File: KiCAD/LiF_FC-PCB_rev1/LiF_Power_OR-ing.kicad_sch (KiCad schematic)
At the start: 16 parts, among them Q1 IRLML6344TRPbF, Q2 IRLML6344TRPbF, U1 LM5050-1, U2 LM5050-1

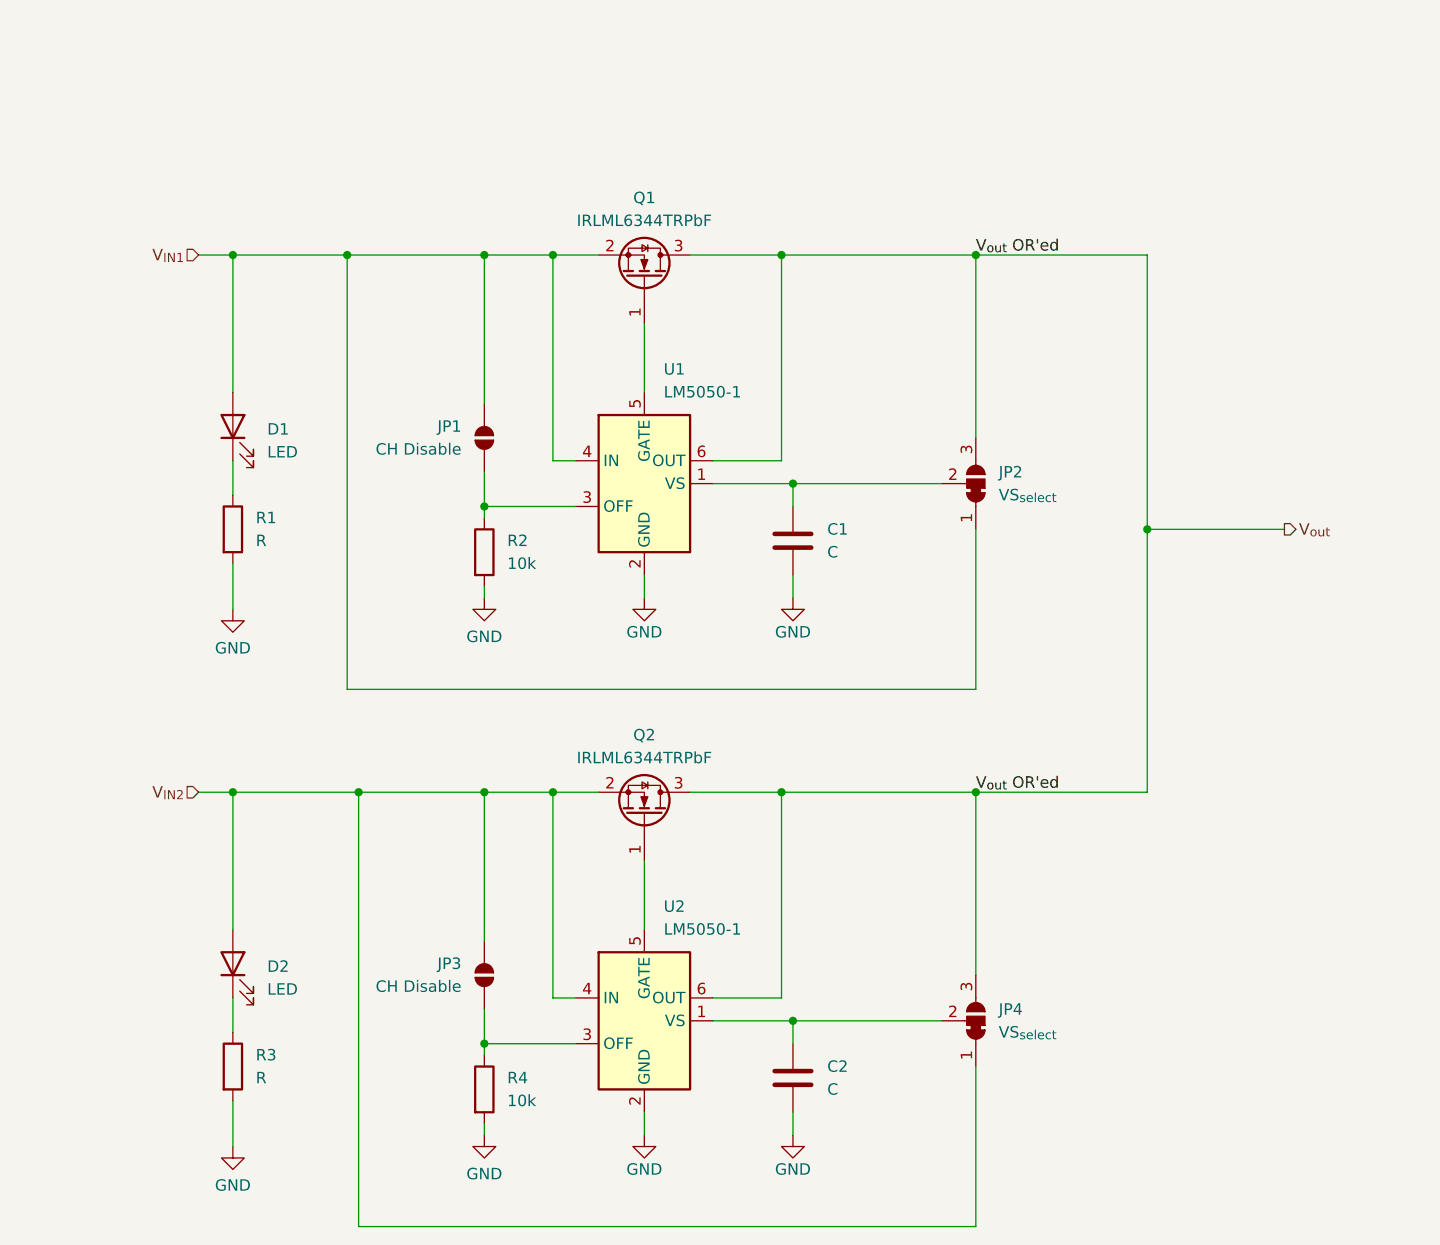
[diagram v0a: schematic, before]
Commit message: reverted 5V reg, reworked power distribution logic, swapped power OR-ing ICs
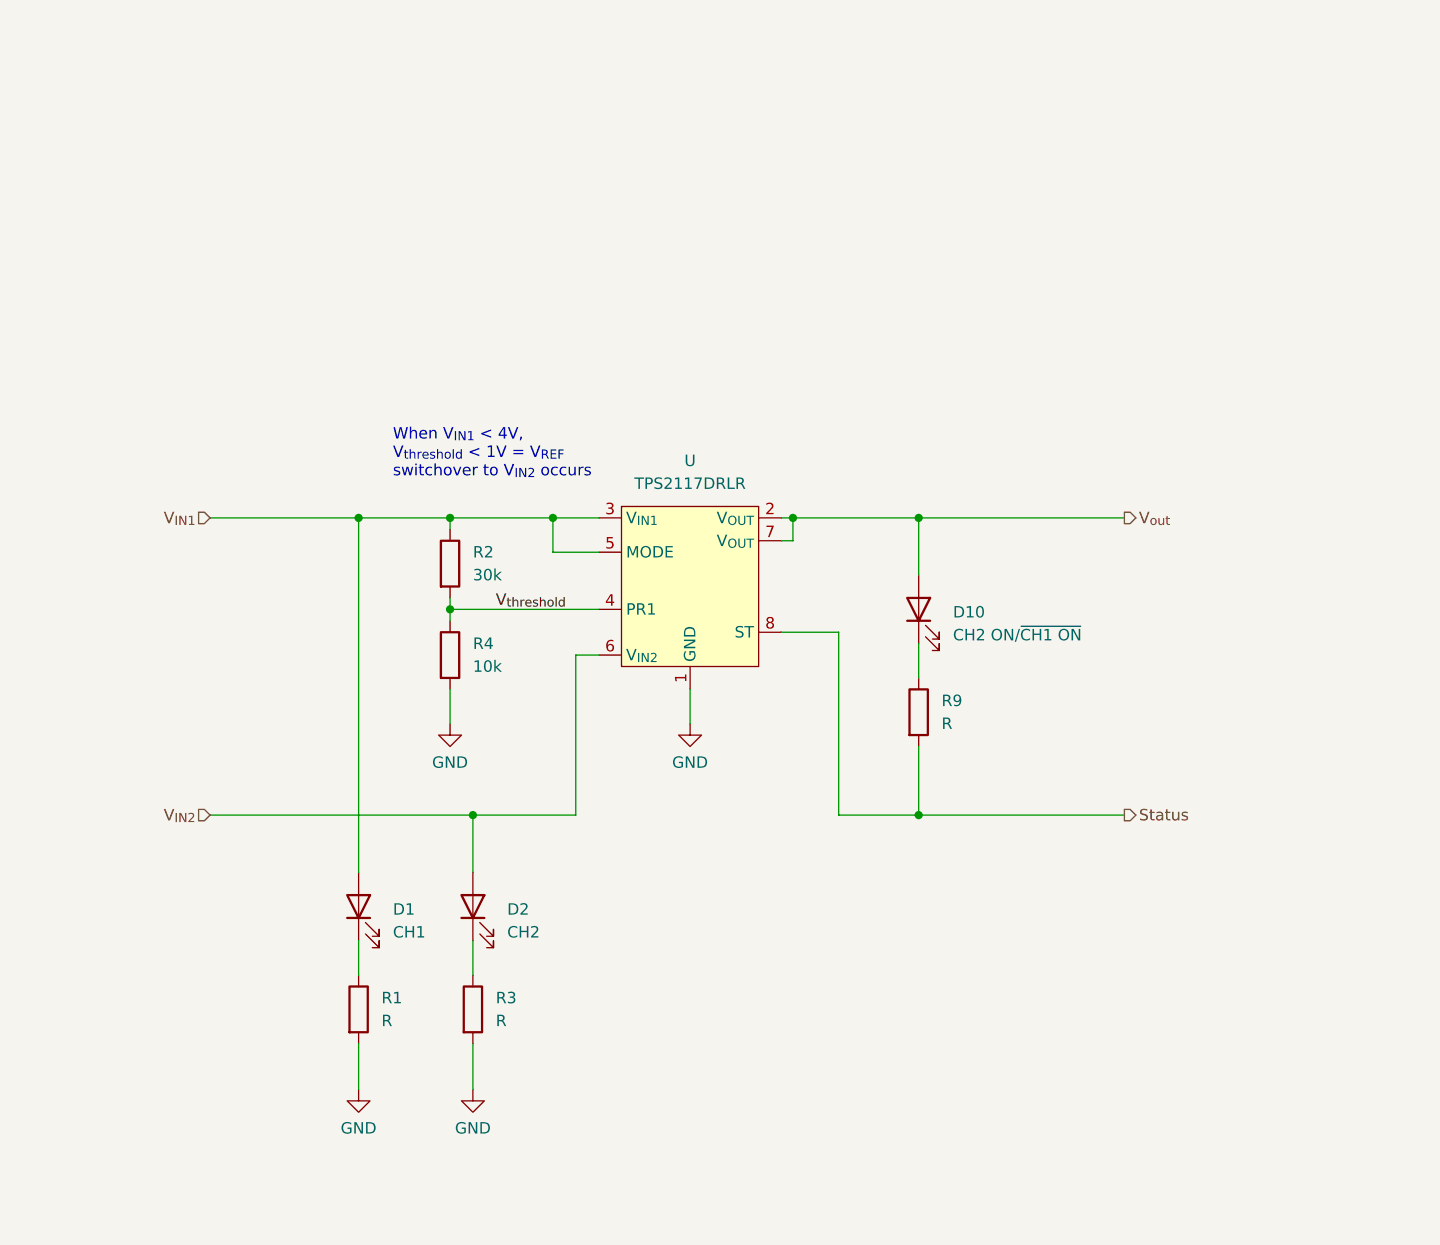
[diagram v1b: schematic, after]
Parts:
- removed C1, C2: C, symbol Device:C
- removed JP1, JP3: CH Disable, symbol Jumper:SolderJumper_2_Open
- removed JP2, JP4: VS_{select}, Jumper:SolderJumper-3_P1.3mm_Bridged12_Pad1.0x1.5mm, symbol Jumper:SolderJumper_3_Bridged12
- removed Q1, Q2: IRLML6344TRPbF, Package_TO_SOT_SMD:SOT-23, symbol Transistor_FET:IRLML6244
- removed U1, U2: LM5050-1, Package_TO_SOT_SMD:TSOT-23-6, symbol Power_Management:LM5050-1
- added D10: CH2 ON/~{CH1 ON}, symbol Device:LED
- added R9: R, symbol Device:R
- added U: TPS2117DRLR, LiF_PCB_Footprints:SOT-5x3_DRL0008A_TEX, symbol LiF_PCB_Symbols:TPS2117
- D1: value LED -> CH1
- D2: value LED -> CH2
- R2: value 10k -> 30k
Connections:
- net GND: now also U.1 (GND); no longer R2.2
- net V_{IN1}: now also R2.1, U.3 (V_{IN1}), U.5 (MODE)
- net V_{IN2}: now also U.6 (V_{IN2})
- net V_{out}: now also D10.2 (A), U.2 (V_{OUT}), U.7 (V_{OUT})
- net V_{threshold}: now reaches R4.1
- net V_{threshold}: now also R2.2, U.4 (PR1)
- new net: D10.1 (K), R9.1
- new net Status: R9.2, U.8 (ST)
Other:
- note added: "When V_{IN1} < 4V, V_{threshold} < 1V = V_{REF} switchover to V_{IN2} occurs"
- moved on the sheet: D1, D2, R1, R3

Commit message: starting to merge Nick's schematics into the main KiCAD project
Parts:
- renumbered U to U?
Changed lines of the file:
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@@
 		(dnp no)
 		(fields_autoplaced yes)
-		(property "Reference" "U"
+		(property "Reference" "U?"
 			(at 146.05 66.04 0)
 			(effects
@@
 		(instances
 			(project "LiF_FC-PCB_rev1"
+				(path "/9e3e8da7-e506-46c9-90e5-307e4ad30d29/dbf56dc2-3990-4801-b0e0-f59d351af64c/b5f6c072-28d6-4dbf-9d97-d5b17dc4e7a5"
+					(reference "U?")
+					(unit 1)
+				)
 				(path "/9e3e8da7-e506-46c9-90e5-307e4ad30d29/dbf56dc2-3990-4801-b0e0-f59d351af64c/d7dd20e9-8027-4523-a1e0-5e82c0dab821"
 					(reference "U3")

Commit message: Finished schematics, mostly. Only MCU sheet left. Doing component sourcing
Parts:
- D3: renamed from D10; footprint (none) -> LED_SMD:LED_0805_2012Metric; DKPN (none) -> 5366-LC170JRCT-U1CT-ND; PN (none) -> LC170JRCT-U1
- D4: renamed from D1; footprint (none) -> LED_SMD:LED_0805_2012Metric; DKPN (none) -> 5366-LC170JRCT-U1CT-ND; PN (none) -> LC170JRCT-U1
- D5: renamed from D2; footprint (none) -> LED_SMD:LED_0805_2012Metric; DKPN (none) -> 5366-LC170JRCT-U1CT-ND; PN (none) -> LC170JRCT-U1
- R12: renamed from R9; value R -> 470; footprint (none) -> Resistor_SMD:R_0805_2012Metric
- R13: renamed from R1; value R -> 470; footprint (none) -> Resistor_SMD:R_0805_2012Metric
- R14: renamed from R3; value R -> 470; footprint (none) -> Resistor_SMD:R_0805_2012Metric
- gave numbers to parts that had none: 1
- renumbered R2 to R10, R4 to R11
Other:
- note added: "Lithium Firefly - Power OR-ing"
- company: (none) -> Lithium Firefly Team

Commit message: Added MCU pinout, shanged shift registers to GPIO expanders to save pins on MCU
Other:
- title: (none) -> Lithium Firefly Custom FC/CC PCB
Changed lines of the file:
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@@
 	(paper "A4")
 	(title_block
+		(title "Lithium Firefly Custom FC/CC PCB")
+		(date "2026-07-11")
 		(rev "1")
 		(company "Lithium Firefly Team")
+		(comment 1 "Designed by MR")
 		(comment 2 "Verified by MR")
 	)
@@
 		(on_board yes)
 		(dnp no)
-		(property "Reference" "#PWR014"
+		(property "Reference" "#PWR018"
 			(at 121.92 142.24 0)
 			(effects
@@
 			(project "LiF_FC-PCB_rev1"
 				(path "/9e3e8da7-e506-46c9-90e5-307e4ad30d29/dbf56dc2-3990-4801-b0e0-f59d351af64c/b5f6c072-28d6-4dbf-9d97-d5b17dc4e7a5"
-					(reference "#PWR014")
+					(reference "#PWR018")
 					(unit 1)
 				)
 				(path "/9e3e8da7-e506-46c9-90e5-307e4ad30d29/dbf56dc2-3990-4801-b0e0-f59d351af64c/d7dd20e9-8027-4523-a1e0-5e82c0dab821"
-					(reference "#PWR018")
+					(reference "#PWR022")
 					(unit 1)
 				)
@@
 		(on_board yes)
 		(dnp no)
-		(property "Reference" "#PWR012"
+		(property "Reference" "#PWR016"
 			(at 146.05 101.6 0)
 			(effects
@@
 			(project "LiF_FC-PCB_rev1"
 				(path "/9e3e8da7-e506-46c9-90e5-307e4ad30d29/dbf56dc2-3990-4801-b0e0-f59d351af64c/b5f6c072-28d6-4dbf-9d97-d5b17dc4e7a5"
-					(reference "#PWR012")
+					(reference "#PWR016")
 					(unit 1)
 				)
 				(path "/9e3e8da7-e506-46c9-90e5-307e4ad30d29/dbf56dc2-3990-4801-b0e0-f59d351af64c/d7dd20e9-8027-4523-a1e0-5e82c0dab821"
-					(reference "#PWR016")
+					(reference "#PWR020")
 					(unit 1)
 				)
@@
 		(on_board yes)
 		(dnp no)
-		(property "Reference" "#PWR013"
+		(property "Reference" "#PWR017"
 			(at 109.22 142.24 0)
 			(effects
@@
 			(project "LiF_FC-PCB_rev1"
 				(path "/9e3e8da7-e506-46c9-90e5-307e4ad30d29/dbf56dc2-3990-4801-b0e0-f59d351af64c/b5f6c072-28d6-4dbf-9d97-d5b17dc4e7a5"
-					(reference "#PWR013")
+					(reference "#PWR017")
 					(unit 1)
 				)
 				(path "/9e3e8da7-e506-46c9-90e5-307e4ad30d29/dbf56dc2-3990-4801-b0e0-f59d351af64c/d7dd20e9-8027-4523-a1e0-5e82c0dab821"
-					(reference "#PWR017")
+					(reference "#PWR021")
 					(unit 1)
 				)
@@
 		(on_board yes)
 		(dnp no)
-		(property "Reference" "#PWR011"
+		(property "Reference" "#PWR015"
 			(at 119.38 101.6 0)
 			(effects
@@
 			(project "LiF_FC-PCB_rev1"
 				(path "/9e3e8da7-e506-46c9-90e5-307e4ad30d29/dbf56dc2-3990-4801-b0e0-f59d351af64c/b5f6c072-28d6-4dbf-9d97-d5b17dc4e7a5"
-					(reference "#PWR011")
+					(reference "#PWR015")
 					(unit 1)
 				)
 				(path "/9e3e8da7-e506-46c9-90e5-307e4ad30d29/dbf56dc2-3990-4801-b0e0-f59d351af64c/d7dd20e9-8027-4523-a1e0-5e82c0dab821"
-					(reference "#PWR015")
-					(unit 1)
-				)
+					(reference "#PWR019")
+					(unit 1)
+				)

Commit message: finished service PCB routing and silkscreen, finished IO PCB layout, routing, and silkscreen. Exported production files, submitted PCB for manufacturing by JLCPCB
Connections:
- net GND: now also D4.1 (K), D5.1 (K); no longer R13.2, R14.2
- net V_{IN1}: now also R13.2; no longer D4.2 (A)
- net V_{IN2}: now also R14.2; no longer D5.2 (A)
- net at R13.1: now also D4.2 (A); no longer D4.1 (K)
- net at R14.1: now also D5.2 (A); no longer D5.1 (K)
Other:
- moved on the sheet: D4, D5, R13, R14
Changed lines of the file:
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@@
 	(symbol
 		(lib_id "Device:LED")
-		(at 109.22 115.57 90)
+		(at 109.22 127 90)
 		(unit 1)
 		(exclude_from_sim no)
@@
 		(fields_autoplaced yes)
 		(property "Reference" "D4"
-			(at 113.03 115.8874 90)
+			(at 113.03 127.3174 90)
 			(effects
 				(font
@@
 		)
 		(property "Value" "CH1"
-			(at 113.03 118.4274 90)
+			(at 113.03 129.8574 90)
 			(effects
 				(font
@@
 		)
 		(property "Footprint" "LED_SMD:LED_0805_2012Metric"
-			(at 109.22 115.57 0)
+			(at 109.22 127 0)
 			(effects
 				(font
@@
 		)
 		(property "Datasheet" "~"
-			(at 109.22 115.57 0)
+			(at 109.22 127 0)
 			(effects
 				(font
@@
 		)
 		(property "Description" "Light emitting diode"
-			(at 109.22 115.57 0)
+			(at 109.22 127 0)
 			(effects
 				(font
@@
 		)
 		(property "Sim.Pins" "1=K 2=A"
-			(at 109.22 115.57 0)
+			(at 109.22 127 0)
 			(effects
 				(font
@@
 		)
 		(property "DKPN" "5366-LC170JRCT-U1CT-ND"
-			(at 109.22 115.57 90)
+			(at 109.22 127 90)
 			(effects
 				(font
@@
 		)
 		(property "PN" "LC170JRCT-U1"
-			(at 109.22 115.57 90)
+			(at 109.22 127 90)
 			(effects
 				(font
@@
 		)
 		(property "CREATOR" ""
-			(at 109.22 115.57 90)
+			(at 109.22 127 90)
 			(effects
 				(font
@@
 		)
 		(property "Check_prices" ""
-			(at 109.22 115.57 90)
+			(at 109.22 127 90)
 			(effects
 				(font
@@
 		)
 		(property "Description_1" ""
-			(at 109.22 115.57 90)
+			(at 109.22 127 90)
 			(effects
 				(font
@@
 		)
 		(property "DigiKey_Part_Number" ""
-			(at 109.22 115.57 90)
+			(at 109.22 127 90)
 			(effects
 				(font
@@
 		)
 		(property "Package" ""
-			(at 109.22 115.57 90)
+			(at 109.22 127 90)
 			(effects
 				(font
@@
 		)
 		(property "SNAPEDA_PN" ""
-			(at 109.22 115.57 90)
+			(at 109.22 127 90)
 			(effects
 				(font
@@
 		)
 		(property "SnapEDA_Link" ""
-			(at 109.22 115.57 90)
+			(at 109.22 127 90)
 			(effects
 				(font
@@
 		)
 		(property "VERIFIER" ""
-			(at 109.22 115.57 90)
+			(at 109.22 127 90)
 			(effects
 				(font
@@
 	(symbol
 		(lib_id "Device:R")
-		(at 121.92 127 0)
+		(at 121.92 115.57 180)
 		(unit 1)
 		(exclude_from_sim no)
@@
 		(fields_autoplaced yes)
 		(property "Reference" "R14"
-			(at 124.46 125.7299 0)
-			(effects
-				(font
-					(size 1.27 1.27)
-				)
-				(justify left)
+			(at 124.46 114.2999 0)
+			(effects
+				(font
+					(size 1.27 1.27)
+				)
+				(justify right)
 			)
 		)
 		(property "Value" "470"
-			(at 124.46 128.2699 0)
-			(effects
-				(font
-					(size 1.27 1.27)
-				)
-				(justify left)
+			(at 124.46 116.8399 0)
+			(effects
+				(font
+					(size 1.27 1.27)
+				)
+				(justify right)
 			)
 		)
 		(property "Footprint" "Resistor_SMD:R_0805_2012Metric"
-			(at 120.142 127 90)
+			(at 123.698 115.57 90)
 			(effects
 				(font
@@
 		)
 		(property "Datasheet" "~"
-			(at 121.92 127 0)
+			(at 121.92 115.57 0)
 			(effects
 				(font
@@
 		)
 		(property "Description" "Resistor"
-			(at 121.92 127 0)
+			(at 121.92 115.57 0)
 			(effects
 				(font
@@
 		)
 		(property "CREATOR" ""
-			(at 121.92 127 0)
+			(at 121.92 115.57 0)
 			(effects
 				(font
@@
 		)
 		(property "Check_prices" ""
-			(at 121.92 127 0)
+			(at 121.92 115.57 0)
 			(effects
 				(font
@@
 		)
 		(property "Description_1" ""
-			(at 121.92 127 0)
+			(at 121.92 115.57 0)
 			(effects
 				(font
@@
 		)
 		(property "DigiKey_Part_Number" ""
-			(at 121.92 127 0)
+			(at 121.92 115.57 0)
 			(effects
 				(font
@@
 		)
 		(property "Package" ""
-			(at 121.92 127 0)
+			(at 121.92 115.57 0)
 			(effects
 				(font
@@
 		)
 		(property "SNAPEDA_PN" ""
-			(at 121.92 127 0)
+			(at 121.92 115.57 0)
 			(effects
 				(font
@@
 		)
 		(property "SnapEDA_Link" ""
-			(at 121.92 127 0)
+			(at 121.92 115.57 0)
 			(effects
 				(font
@@
 		)
 		(property "VERIFIER" ""
-			(at 121.92 127 0)
+			(at 121.92 115.57 0)
 			(effects
 				(font
@@
 	(symbol
 		(lib_id "Device:LED")
-		(at 121.92 115.57 90)
+		(at 121.92 127 90)
 		(unit 1)
 		(exclude_from_sim no)
@@
 		(fields_autoplaced yes)
 		(property "Reference" "D5"
-			(at 125.73 115.8874 90)
+			(at 125.73 127.3174 90)
 			(effects
 				(font
@@
 		)
 		(property "Value" "CH2"
-			(at 125.73 118.4274 90)
+			(at 125.73 129.8574 90)
 			(effects
 				(font
@@
 		)
 		(property "Footprint" "LED_SMD:LED_0805_2012Metric"
-			(at 121.92 115.57 0)
+			(at 121.92 127 0)
 			(effects
 				(font
@@
 		)
 		(property "Datasheet" "~"
-			(at 121.92 115.57 0)
+			(at 121.92 127 0)
 			(effects
 				(font
@@
 		)
 		(property "Description" "Light emitting diode"
-			(at 121.92 115.57 0)
+			(at 121.92 127 0)
 			(effects
 				(font
@@
 		)
 		(property "Sim.Pins" "1=K 2=A"
-			(at 121.92 115.57 0)
+			(at 121.92 127 0)
 			(effects
 				(font
@@
 		)
 		(property "DKPN" "5366-LC170JRCT-U1CT-ND"
-			(at 121.92 115.57 90)
+			(at 121.92 127 90)
 			(effects
 				(font
@@
 		)
 		(property "PN" "LC170JRCT-U1"
-			(at 121.92 115.57 90)
+			(at 121.92 127 90)
 			(effects
 				(font
@@
 		)
 		(property "CREATOR" ""
-			(at 121.92 115.57 90)
+			(at 121.92 127 90)
 			(effects
 				(font
@@
 		)
 		(property "Check_prices" ""
-			(at 121.92 115.57 90)
+			(at 121.92 127 90)
 			(effects
 				(font
@@
 		)
 		(property "Description_1" ""
-			(at 121.92 115.57 90)
+			(at 121.92 127 90)
 			(effects
 				(font
@@
 		)
 		(property "DigiKey_Part_Number" ""
-			(at 121.92 115.57 90)
+			(at 121.92 127 90)
 			(effects
 				(font
@@
 		)
 		(property "Package" ""
-			(at 121.92 115.57 90)
+			(at 121.92 127 90)
 			(effects
 				(font
@@
 		)
 		(property "SNAPEDA_PN" ""
-			(at 121.92 115.57 90)
+			(at 121.92 127 90)
 			(effects
 				(font
@@
 		)
 		(property "SnapEDA_Link" ""
-			(at 121.92 115.57 90)
+			(at 121.92 127 90)
 			(effects
 				(font
@@
 		)
 		(property "VERIFIER" ""
-			(at 121.92 115.57 90)
+			(at 121.92 127 90)
 			(effects
 				(font
@@
 	(symbol
 		(lib_id "Device:R")
-		(at 109.22 127 0)
+		(at 109.22 115.57 180)
 		(unit 1)
 		(exclude_from_sim no)
@@
 		(fields_autoplaced yes)
 		(property "Reference" "R13"
-			(at 111.76 125.7299 0)
-			(effects
-				(font
-					(size 1.27 1.27)
-				)
-				(justify left)
+			(at 111.76 114.2999 0)
+			(effects
+				(font
+					(size 1.27 1.27)
+				)
+				(justify right)
 			)
 		)
 		(property "Value" "470"
-			(at 111.76 128.2699 0)
-			(effects
-				(font
-					(size 1.27 1.27)
-				)
-				(justify left)
+			(at 111.76 116.8399 0)
+			(effects
+				(font
+					(size 1.27 1.27)
+				)
+				(justify right)
 			)
 		)
 		(property "Footprint" "Resistor_SMD:R_0805_2012Metric"
-			(at 107.442 127 90)
+			(at 110.998 115.57 90)
 			(effects
 				(font
@@
 		)
 		(property "Datasheet" "~"
-			(at 109.22 127 0)
+			(at 109.22 115.57 0)
 			(effects
 				(font
@@
 		)
 		(property "Description" "Resistor"
-			(at 109.22 127 0)
+			(at 109.22 115.57 0)
 			(effects
 				(font
@@
 		)
 		(property "CREATOR" ""
-			(at 109.22 127 0)
+			(at 109.22 115.57 0)
 			(effects
 				(font
@@
 		)
 		(property "Check_prices" ""
-			(at 109.22 127 0)
+			(at 109.22 115.57 0)
 			(effects
 				(font
@@
 		)
 		(property "Description_1" ""
-			(at 109.22 127 0)
+			(at 109.22 115.57 0)
 			(effects
 				(font
@@
 		)
 		(property "DigiKey_Part_Number" ""
-			(at 109.22 127 0)
+			(at 109.22 115.57 0)
 			(effects
 				(font
@@
 		)
 		(property "Package" ""
-			(at 109.22 127 0)
+			(at 109.22 115.57 0)
 			(effects
 				(font
@@
 		)
 		(property "SNAPEDA_PN" ""
-			(at 109.22 127 0)
+			(at 109.22 115.57 0)
 			(effects
 				(font
@@
 		)
 		(property "SnapEDA_Link" ""
-			(at 109.22 127 0)
+			(at 109.22 115.57 0)
 			(effects
 				(font
@@
 		)
 		(property "VERIFIER" ""
-			(at 109.22 127 0)
-			(effects
-				(font
+			(at 109.22 115.57 0)
+			(effects
+				(font
